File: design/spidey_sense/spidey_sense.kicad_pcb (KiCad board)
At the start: 2 copper layers, 63.5 x 46.5 mm, 14 parts, among them J1 Input_Screw_Terminal, J10 Output_Screw_Terminal, J2 Thermocouple_Terminal, J3 Thermocouple_Terminal, J4 Thermocouple_Terminal, J5 Thermocouple_Terminal, J6 Conn_01x06_Female, J7 Conn_01x06_Female, J8 Conn_01x06_Female, J9 Conn_01x06_Female

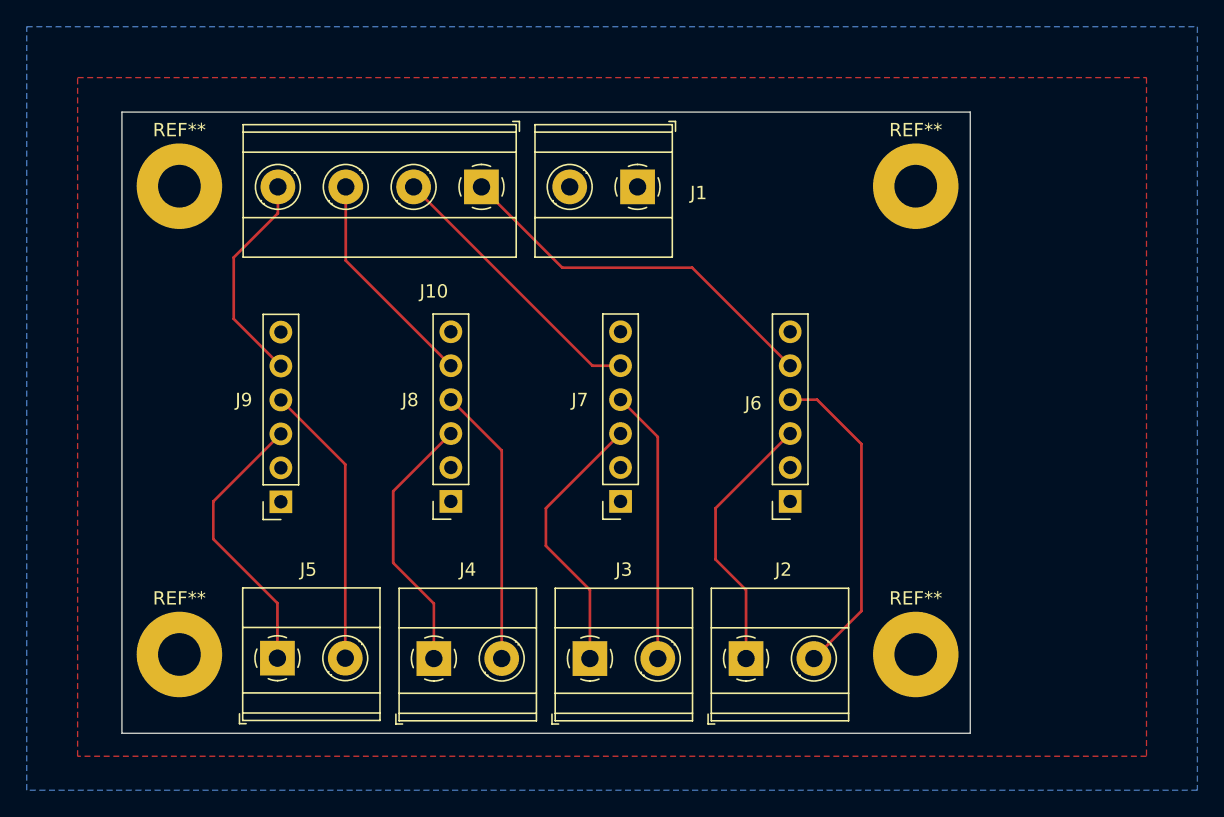
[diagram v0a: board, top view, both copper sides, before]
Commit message: Changed pin header orientations and added silkscreen labels
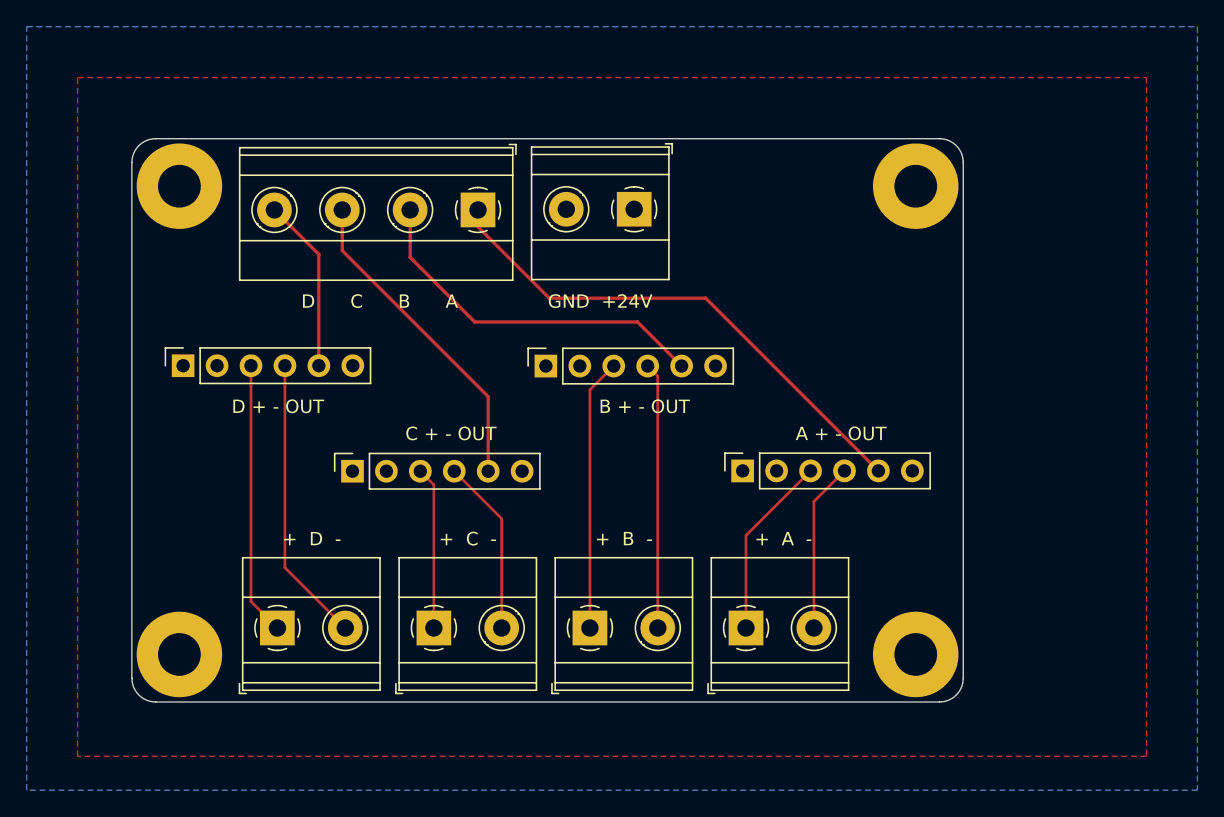
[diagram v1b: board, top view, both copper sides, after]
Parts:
- moved J9 12.5 mm to (51.1, 80.0), turned to 90 degrees
- moved J7 11.6 mm to (78.2, 80.0), turned to 90 degrees
- moved J8 7.71 mm to (63.8, 87.9), turned to 90 degrees
- moved J6 4.23 mm to (93.0, 87.9), turned to 90 degrees
- moved J2 2.29 mm to (93.2, 99.6)
- moved J3 2.29 mm to (81.5, 99.6)
- moved J4 2.29 mm to (69.8, 99.6)
- moved J5 2.26 mm to (58.1, 99.6)
- moved J10 1.75 mm to (73.2, 68.3)
- moved J1 1.69 mm to (84.8, 68.3)
- renumbered REF** to REF
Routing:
- net /A-: track 24.2 -> 12.7 mm
- net /Aout: track 28.7 -> 38.8 mm
- net /C-: track 21.0 -> 13.2 mm
- net /C+: track 19.9 -> 12.2 mm
- net /Cout: track 16.6 -> 24.1 mm
- net /A+: track 20.1 -> 13.8 mm
- net /Bout: track 21.0 -> 27.2 mm
- net /Dout: track 16.2 -> 13.0 mm
- net /B-: track 20.5 -> 19.9 mm
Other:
- board size 63.5 x 46.5 mm -> 62.2 x 42.2 mm
- board text added: "+ A -"
- board text added: "+ B -"
- board text added: "+ C -"
- board text added: "+ D -"
- board text added: "A + - OUT"
- board text added: "B + - OUT"
- board text added: "C + - OUT"
- board text added: "D + - OUT"
- board text added: "D C B A"
- board text added: "GND +24V"

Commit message: Added board info and logo
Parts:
- added G***: LOGO, Team_Logo:Logo_SilkScreen_10mm, F.Cu at (95.2, 68.8)
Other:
- board text added: "10/25/2022"
- board text added: "Ozayr Raazi"
- board text added: "Spidey Sense"
